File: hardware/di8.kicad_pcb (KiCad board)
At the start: 4 copper layers, 100 x 85 mm, 106 parts, among them J101 TNG-Power-TOP, J102 TNG-Power-BTM, J103 TNG-Data-TOP, J104 TNG-Data-BTM, P101 BOOT, P102 Debug, P201 INPUT0, P202 INPUT1, P203 INPUT2, P204 INPUT3, U101 STM32F070CBT6, U102 AP7333, U103 82400152, U104 PDQE10, U201 ISO1212, U202 ISO1212, U203 ISO1212, U204 ISO1212, X101 TBD

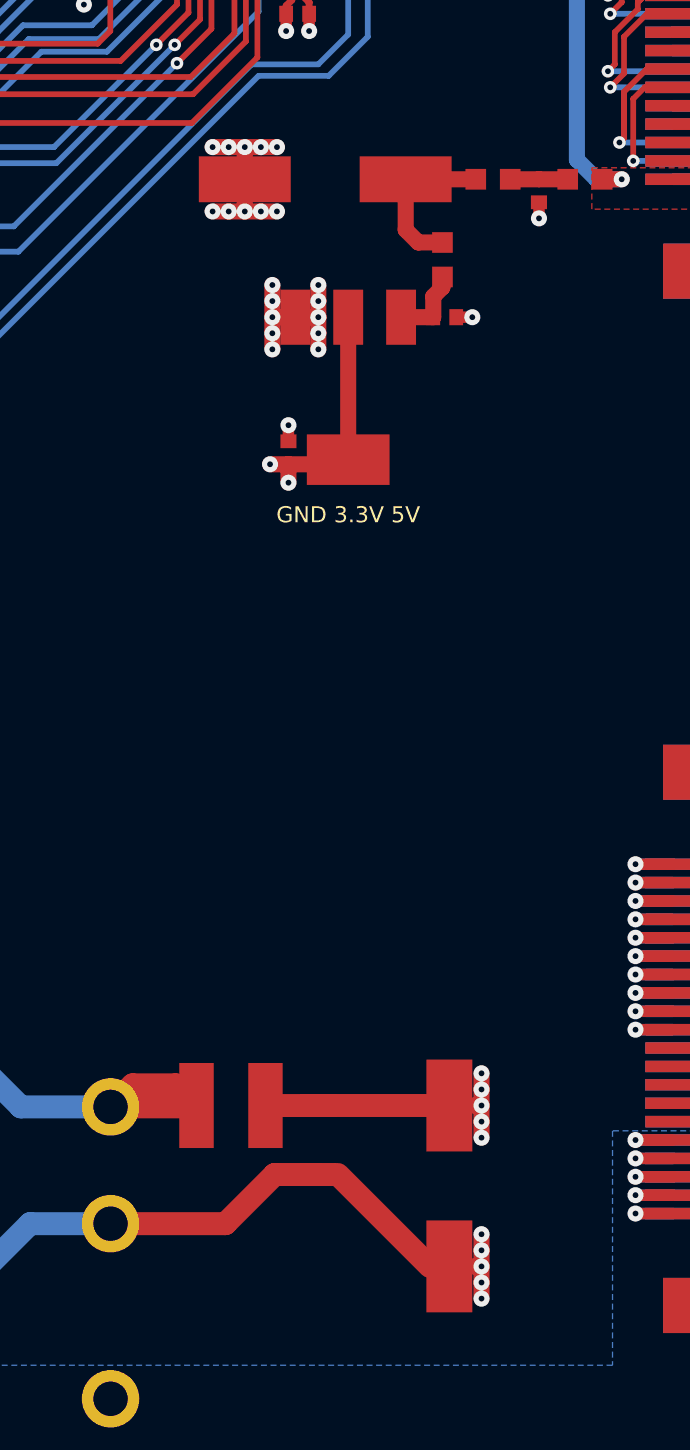
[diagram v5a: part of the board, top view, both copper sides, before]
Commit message: routing improvement, ordered version 1.0
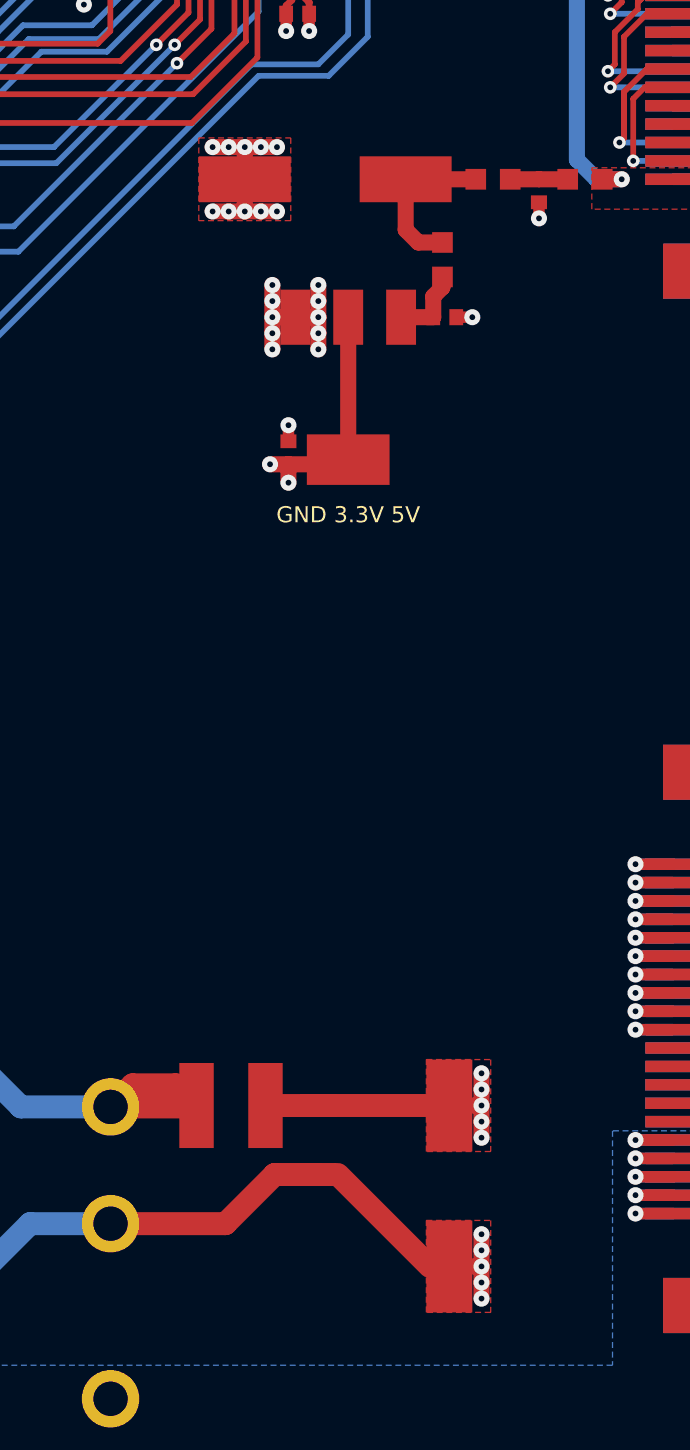
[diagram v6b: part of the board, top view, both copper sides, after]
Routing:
- added copper zone on F.Cu, net AGNDA
- added copper zone on F.Cu, net GND
- added copper zone on F.Cu, net VCCPWRA

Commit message: add hints
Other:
- board text added: "Add 24V Fuse"
- board text added: "FIX Footprint"
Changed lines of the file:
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@@
   (general
     (thickness 1.6)
-    (drawings 22)
+    (drawings 24)
     (tracks 1273)
     (zones 0)
@@
     (47 F.CrtYd user)
     (48 B.Fab user)
-    (49 F.Fab user hide)
+    (49 F.Fab user)
   )
   (setup
@@
     (pad_drill 0.6)
     (pad_to_mask_clearance 0)
+    (solder_mask_min_width 0.25)
     (aux_axis_origin 189.8 62.5)
     (grid_origin 189.8 62.5)
-    (visible_elements FFFEFF7F)
+    (visible_elements FFFFFF7F)
     (pcbplotparams
       (layerselection 0x010fc_ffffffff)
@@
       (net 96 "Net-(P102-Pad1)"))
   )
+  (gr_text "Add 24V Fuse" (at 143.1 119.4) (layer Dwgs.User)
+    (effects (font (size 4 4) (thickness 0.3)))
+  )
+  (gr_text "FIX Footprint" (at 163.2 106.2) (layer Dwgs.User)
+    (effects (font (size 2 2) (thickness 0.3)))
+  )
   (gr_text "GND 3.3V 5V" (at 163.4 104.7) (layer F.SilkS)

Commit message: add another hint
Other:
- board text added: "Fix unidirectional -> bidirection Diodes"
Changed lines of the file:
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@@
   (general
     (thickness 1.6)
-    (drawings 24)
+    (drawings 25)
     (tracks 1273)
     (zones 0)
@@
       (net 96 "Net-(P102-Pad1)"))
   )
+  (gr_text "Fix unidirectional -> bidirection Diodes" (at 103.1 97.4) (layer Dwgs.User)
+    (effects (font (size 3 3) (thickness 0.3)))
+  )
   (gr_text "Add 24V Fuse" (at 143.1 119.4) (layer Dwgs.User)
